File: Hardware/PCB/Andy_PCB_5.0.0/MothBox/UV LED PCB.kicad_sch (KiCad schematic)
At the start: 24 parts, among them P4 External Attractor, Q10 BC817, Q11 BC817, Q8 BC817, Q9 BC817, U10 IRF9335TRPBF, U11 IRF9335TRPBF, U12 IRF9335TRPBF, U13 IRF9335TRPBF

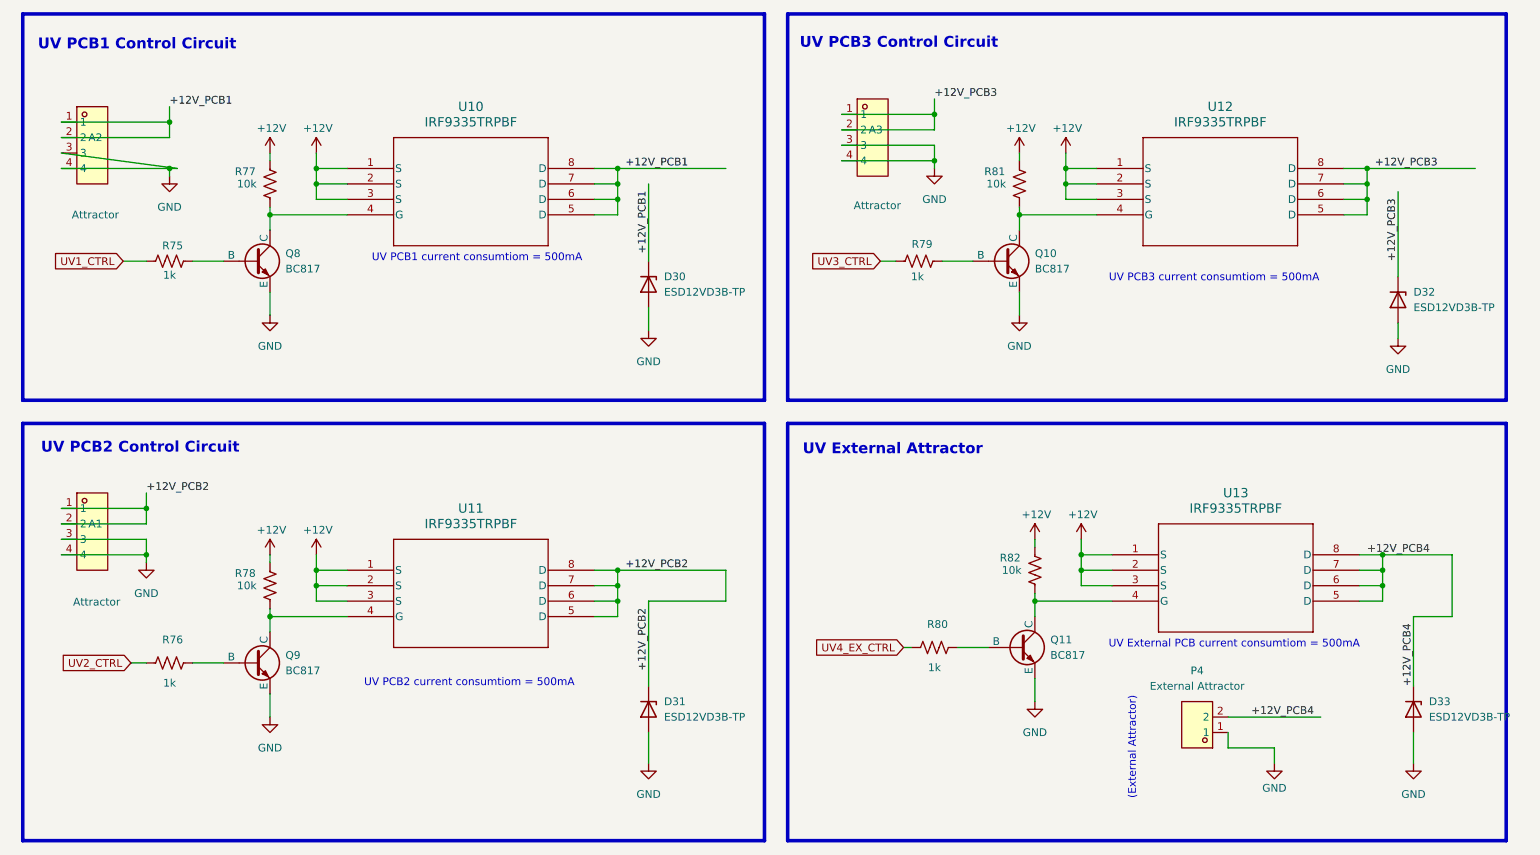
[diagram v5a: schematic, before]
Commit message: Fixed parts with conflicting LCSC footprints
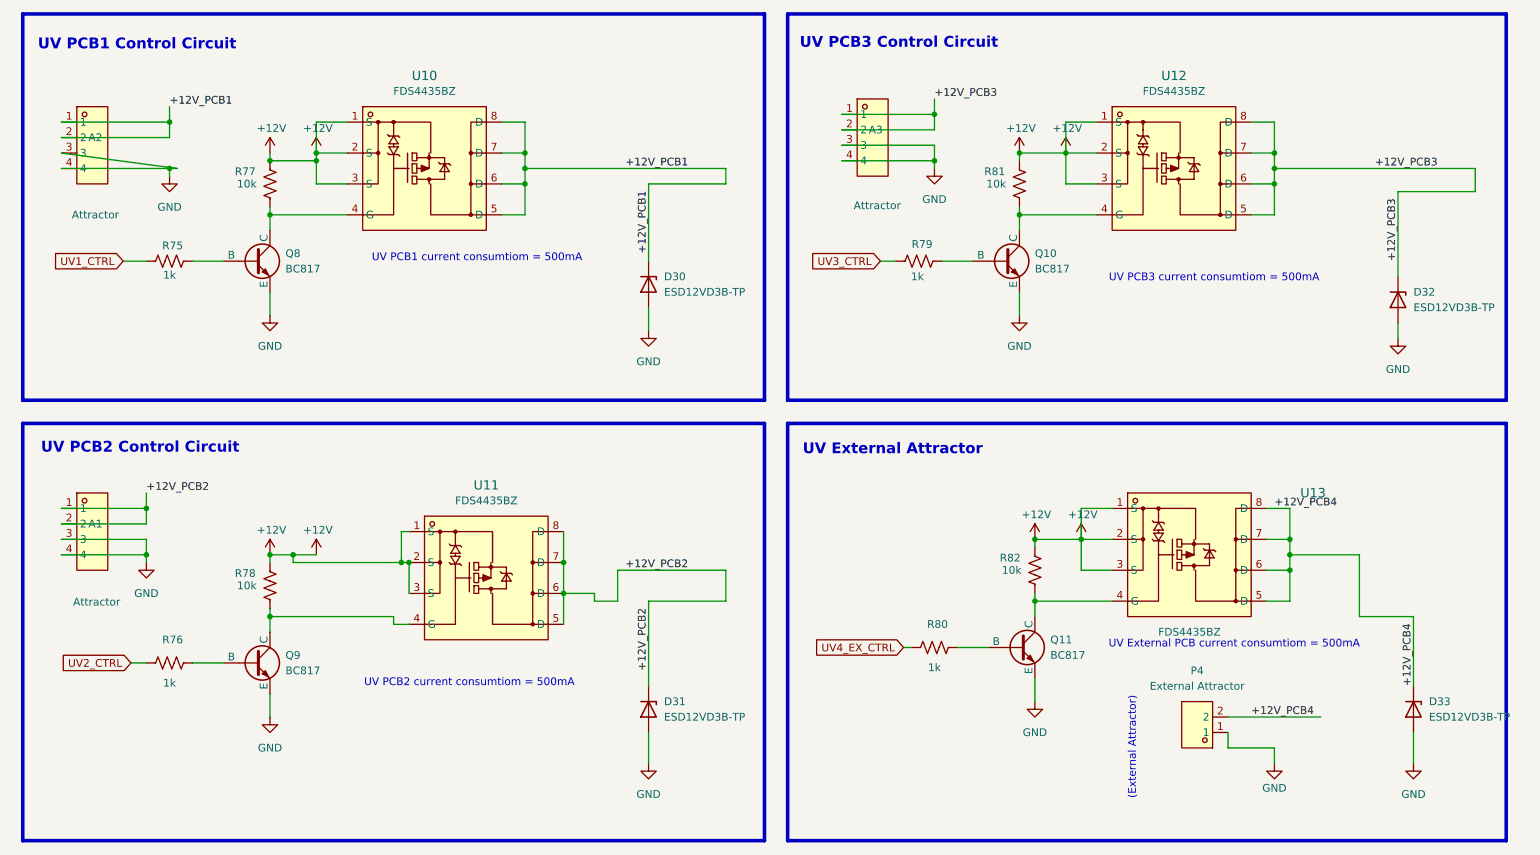
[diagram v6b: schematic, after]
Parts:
- U10, U11, U12, U13: value IRF9335TRPBF -> FDS4435BZ; footprint Package_SO:SOIC-8_3.9x4.9mm_P1.27mm -> easyeda2kicad:SOIC-8_L5.0-W4.0-P1.27-LS6.0-BL; symbol 2025-05-03_11-59-41:IRF9335TRPBF -> easyeda2kicad:FDS4435BZ; Digikey Part No IRF9335TRPBF -> (none); LCSC Part (none) -> C23931; LCSC Part no  C41355033 -> (none)

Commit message: Final changes footprints before JLC
c1 - rotate left 180

e3 - rotate left 180

q1 rotate l 180

U1,U2,U6,U7 rotate 180

u5 Epaper header - 90 right

u16 - NOT RIGHT ANGLE should be C2897440  or C22373943
d30 they might be bidirectional

Q10,Q11,Q4,Q6,Q8,Q9

C39828
rotate 180
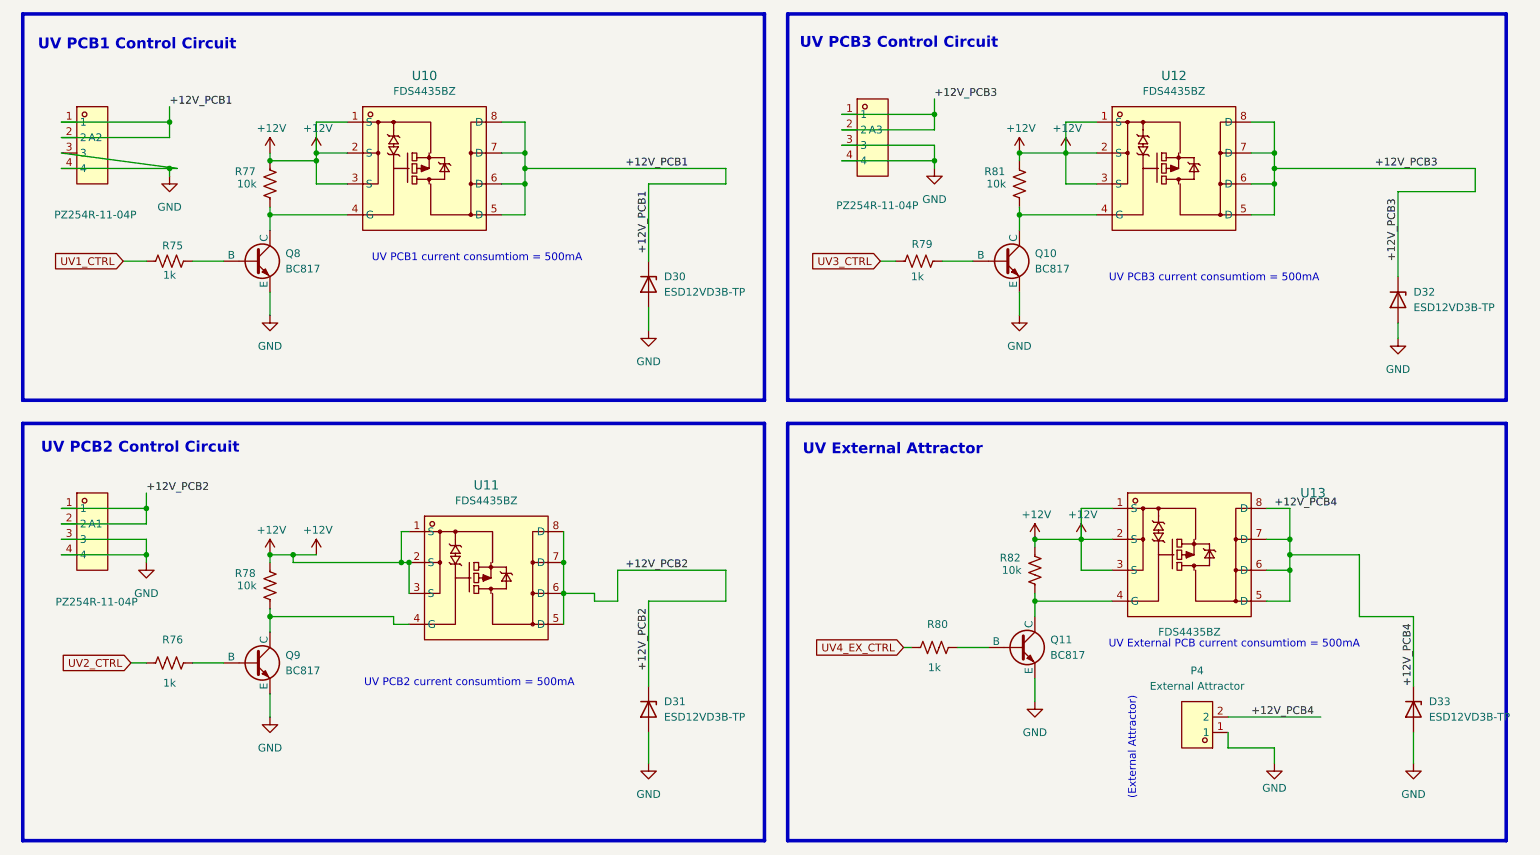
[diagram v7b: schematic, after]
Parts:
- A1, A2, A3: value Attractor -> PZ254R-11-04P; footprint Attractor:HDR-TH_4P-P2.54-H-M-W10.4 -> easyeda2kicad:HDR-TH_4P-P2.54-H-M-W10.4; LCSC Part no  C49661 -> (none)
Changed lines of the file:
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@@
 			)
 		)
-		(property "Value" "Attractor"
+		(property "Value" "PZ254R-11-04P"
 			(at 38.608 60.96 0)
 			(effects
@@
 			)
 		)
-		(property "Footprint" "Attractor:HDR-TH_4P-P2.54-H-M-W10.4"
+		(property "Footprint" "easyeda2kicad:HDR-TH_4P-P2.54-H-M-W10.4"
 			(at 38.1 60.96 0)
 			(effects
@@
 				)
 				(hide yes)
-			)
-		)
-		(property "LCSC Part no " "C49661"
-			(at 38.1 49.53 0)
-			(effects
-				(font
-					(size 1.27 1.27)
-				)
-				(hide yes)
-			)
-		)
-		(property "LCSC PN" ""
-			(at 38.1 49.53 0)
-			(effects
-				(font
-					(size 1.27 1.27)
-				)
 			)
 		)
@@
 			)
 		)
-		(property "Value" "Attractor"
+		(property "Value" "PZ254R-11-04P"
 			(at 38.8165 124.5959 0)
 			(effects
@@
 			)
 		)
-		(property "Footprint" "Attractor:HDR-TH_4P-P2.54-H-M-W10.4"
+		(property "Footprint" "easyeda2kicad:HDR-TH_4P-P2.54-H-M-W10.4"
 			(at 38.1 124.46 0)
 			(effects
@@
 				)
 				(hide yes)
-			)
-		)
-		(property "LCSC Part no " "C49661"
-			(at 38.1 113.03 0)
-			(effects
-				(font
-					(size 1.27 1.27)
-				)
-				(hide yes)
-			)
-		)
-		(property "LCSC PN" ""
-			(at 38.1 113.03 0)
-			(effects
-				(font
-					(size 1.27 1.27)
-				)
 			)
 		)
@@
 			)
 		)
-		(property "Value" "Attractor"
+		(property "Value" "PZ254R-11-04P"
 			(at 167.132 59.436 0)
 			(effects
@@
 			)
 		)
-		(property "Footprint" "Attractor:HDR-TH_4P-P2.54-H-M-W10.4"
+		(property "Footprint" "easyeda2kicad:HDR-TH_4P-P2.54-H-M-W10.4"
 			(at 166.37 59.69 0)
 			(effects
@@
 			)
 		)
-		(property "LCSC Part no " "C49661"
-			(at 166.37 48.26 0)
-			(effects
-				(font
-					(size 1.27 1.27)
-				)
-				(hide yes)
-			)
-		)
-		(property "LCSC PN" ""
-			(at 166.37 48.26 0)
-			(effects
-				(font
-					(size 1.27 1.27)
-				)
-			)
-		)

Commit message: Maybe these files needed saving too for paul?
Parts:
- A1, A2, A3: symbol attractor_AQ:PZ254R-11-04P -> MB_Library:PZ254R-11-04P
- D30, D31, D32, D33: symbol Diode:ESD5Zxx -> MB_Library:ESD5Zxx
- P4: symbol easyeda2kicad:DB142R-5.08-2P -> MB_Library:DB142R-5.08-2P
- Q10, Q11, Q8, Q9: symbol BC817:BC817_NPN_BJT -> MB_Library:BC817_NPN_BJT
- R75, R76, R77, R78, R79, R80, R81, R82: symbol Device:R_US -> MB_Library:R_US
- U10, U11, U12, U13: symbol easyeda2kicad:FDS4435BZ -> MB_Library:FDS4435BZ
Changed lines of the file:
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@@
 	)
 	(symbol
-		(lib_id "easyeda2kicad:FDS4435BZ")
+		(lib_id "MB_Library:FDS4435BZ")
 		(at 215.9 53.34 0)
 		(unit 1)
@@
 	)
 	(symbol
-		(lib_id "power:GND")
+		(lib_id "MB_Library:GND")
 		(at 129.54 80.01 0)
 		(unit 1)
@@
 	)
 	(symbol
-		(lib_id "BC817:BC817_NPN_BJT")
+		(lib_id "MB_Library:BC817_NPN_BJT")
 		(at 64.77 68.58 0)
 		(unit 1)
@@
 	)
 	(symbol
-		(lib_id "Device:R_US")
+		(lib_id "MB_Library:R_US")
 		(at 190.5 55.88 180)
 		(unit 1)
@@
 	)
 	(symbol
-		(lib_id "power:+12V")
+		(lib_id "MB_Library:+12V")
 		(at 200.66 114.3 0)
 		(unit 1)
@@
 	)
 	(symbol
-		(lib_id "easyeda2kicad:DB142R-5.08-2P")
+		(lib_id "MB_Library:DB142R-5.08-2P")
 		(at 219.71 144.78 180)
 		(unit 1)
@@
 	)
 	(symbol
-		(lib_id "power:+12V")
+		(lib_id "MB_Library:+12V")
 		(at 67.31 116.84 0)
 		(unit 1)
@@
 	)
 	(symbol
-		(lib_id "power:GND")
+		(lib_id "MB_Library:GND")
 		(at 190.5 77.47 0)
 		(unit 1)
@@
 	)
 	(symbol
-		(lib_id "power:GND")
+		(lib_id "MB_Library:GND")
 		(at 252.73 81.28 0)
 		(unit 1)
@@
 	)
 	(symbol
-		(lib_id "BC817:BC817_NPN_BJT")
+		(lib_id "MB_Library:BC817_NPN_BJT")
 		(at 64.77 134.62 0)
 		(unit 1)
@@
 	)
 	(symbol
-		(lib_id "power:GND")
+		(lib_id "MB_Library:GND")
 		(at 67.31 77.47 0)
 		(unit 1)
@@
 	)
 	(symbol
-		(lib_id "Diode:ESD5Zxx")
+		(lib_id "MB_Library:ESD5Zxx")
 		(at 129.54 142.24 270)
 		(unit 1)
@@
 	)
 	(symbol
-		(lib_id "power:+12V")
+		(lib_id "MB_Library:+12V")
 		(at 198.12 50.8 0)
 		(unit 1)
@@
 	)
 	(symbol
-		(lib_id "power:+12V")
+		(lib_id "MB_Library:+12V")
 		(at 74.93 50.8 0)
 		(unit 1)
@@
 	)
 	(symbol
-		(lib_id "Device:R_US")
+		(lib_id "MB_Library:R_US")
 		(at 50.8 134.62 270)
 		(unit 1)
@@
 	)
 	(symbol
-		(lib_id "Device:R_US")
+		(lib_id "MB_Library:R_US")
 		(at 50.8 68.58 270)
 		(unit 1)
@@
 	)
 	(symbol
-		(lib_id "power:+12V")
+		(lib_id "MB_Library:+12V")
 		(at 190.5 50.8 0)
 		(unit 1)
@@
 	)
 	(symbol
-		(lib_id "attractor_AQ:PZ254R-11-04P")
+		(lib_id "MB_Library:PZ254R-11-04P")
 		(at 38.1 49.53 0)
 		(unit 1)
@@
 	)
 	(symbol
-		(lib_id "easyeda2kicad:FDS4435BZ")
+		(lib_id "MB_Library:FDS4435BZ")
 		(at 218.44 116.84 0)
 		(unit 1)
@@
 	)
 	(symbol
-		(lib_id "power:GND")
+		(lib_id "MB_Library:GND")
 		(at 129.54 151.13 0)
 		(unit 1)
@@
 	)
 	(symbol
-		(lib_id "power:GND")
+		(lib_id "MB_Library:GND")
 		(at 46.99 118.11 0)
 		(unit 1)
@@
 	)
 	(symbol
-		(lib_id "Device:R_US")
+		(lib_id "MB_Library:R_US")
 		(at 176.53 132.08 270)
 		(unit 1)
@@
 	)
 	(symbol
-		(lib_id "power:GND")
+		(lib_id "MB_Library:GND")
 		(at 50.8 54.61 0)
 		(unit 1)
@@
 	)
 	(symbol
-		(lib_id "BC817:BC817_NPN_BJT")
+		(lib_id "MB_Library:BC817_NPN_BJT")
 		(at 187.96 68.58 0)
 		(unit 1)
@@
 	)
 	(symbol
-		(lib_id "Device:R_US")
+		(lib_id "MB_Library:R_US")
 		(at 67.31 121.92 180)
 		(unit 1)
@@
 	)
 	(symbol
-		(lib_id "Diode:ESD5Zxx")
+		(lib_id "MB_Library:ESD5Zxx")
 		(at 252.73 74.93 270)
 		(unit 1)
@@
 	)
 	(symbol
-		(lib_id "power:GND")
+		(lib_id "MB_Library:GND")
 		(at 176.53 53.34 0)
 		(unit 1)
@@
 	)
 	(symbol
-		(lib_id "Diode:ESD5Zxx")
+		(lib_id "MB_Library:ESD5Zxx")
 		(at 129.54 72.39 270)
 		(unit 1)
@@
 	)
 	(symbol
-		(lib_id "power:GND")
+		(lib_id "MB_Library:GND")
 		(at 193.04 140.97 0)
 		(unit 1)
@@
 	)
 	(symbol
-		(lib_id "power:+12V")
+		(lib_id "MB_Library:+12V")
 		(at 74.93 116.84 0)
 		(unit 1)
@@
 	)
 	(symbol
-		(lib_id "Device:R_US")
+		(lib_id "MB_Library:R_US")
 		(at 193.04 119.38 180)
 		(unit 1)
@@
 	)
 	(symbol
-		(lib_id "power:+12V")
+		(lib_id "MB_Library:+12V")
 		(at 193.04 114.3 0)
 		(unit 1)
@@
 	)
 	(symbol
-		(lib_id "attractor_AQ:PZ254R-11-04P")
+		(lib_id "MB_Library:PZ254R-11-04P")
 		(at 38.1 113.03 0)
 		(unit 1)
@@
 	)
 	(symbol
-		(lib_id "easyeda2kicad:FDS4435BZ")
+		(lib_id "MB_Library:FDS4435BZ")
 		(at 92.71 53.34 0)
 		(unit 1)
@@
 	)
 	(symbol
-		(lib_id "BC817:BC817_NPN_BJT")
+		(lib_id "MB_Library:BC817_NPN_BJT")
 		(at 190.5 132.08 0)
 		(unit 1)
@@
 	)
 	(symbol
-		(lib_id "attractor_AQ:PZ254R-11-04P")
+		(lib_id "MB_Library:PZ254R-11-04P")
 		(at 166.37 48.26 0)
 		(unit 1)
@@
 	)
 	(symbol
-		(lib_id "Diode:ESD5Zxx")
+		(lib_id "MB_Library:ESD5Zxx")
 		(at 255.27 142.24 270)
 		(unit 1)
@@
 	)
 	(symbol
-		(lib_id "Device:R_US")
+		(lib_id "MB_Library:R_US")
 		(at 173.99 68.58 270)
 		(unit 1)
@@
 	)
 	(symbol
-		(lib_id "power:GND")
+		(lib_id "MB_Library:GND")
 		(at 67.31 143.51 0)
 		(unit 1)
@@
 	)
 	(symbol
-		(lib_id "easyeda2kicad:FDS4435BZ")
+		(lib_id "MB_Library:FDS4435BZ")
 		(at 102.87 120.65 0)
 		(unit 1)
@@
 	)
 	(symbol
-		(lib_id "power:GND")
+		(lib_id "MB_Library:GND")
 		(at 255.27 151.13 0)
 		(unit 1)
@@
 	)
 	(symbol
-		(lib_id "power:+12V")
+		(lib_id "MB_Library:+12V")
 		(at 67.31 50.8 0)
 		(unit 1)
@@
 	)
 	(symbol
-		(lib_id "power:GND")
+		(lib_id "MB_Library:GND")
 		(at 232.41 151.13 0)
 		(unit 1)
@@
 	)
 	(symbol
-		(lib_id "Device:R_US")
+		(lib_id "MB_Library:R_US")
 		(at 67.31 55.88 180)
 		(unit 1)
